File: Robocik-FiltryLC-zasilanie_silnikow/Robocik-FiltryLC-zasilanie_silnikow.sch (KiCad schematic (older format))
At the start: 18 parts, among them J1 XT90PW-F, J2 Conn_01x05, J3 Conn_01x03, J4 Conn_01x03, J5 Conn_01x03, J6 Conn_01x03, U1 ESC, U2 ESC, U3 ESC, U4 ESC

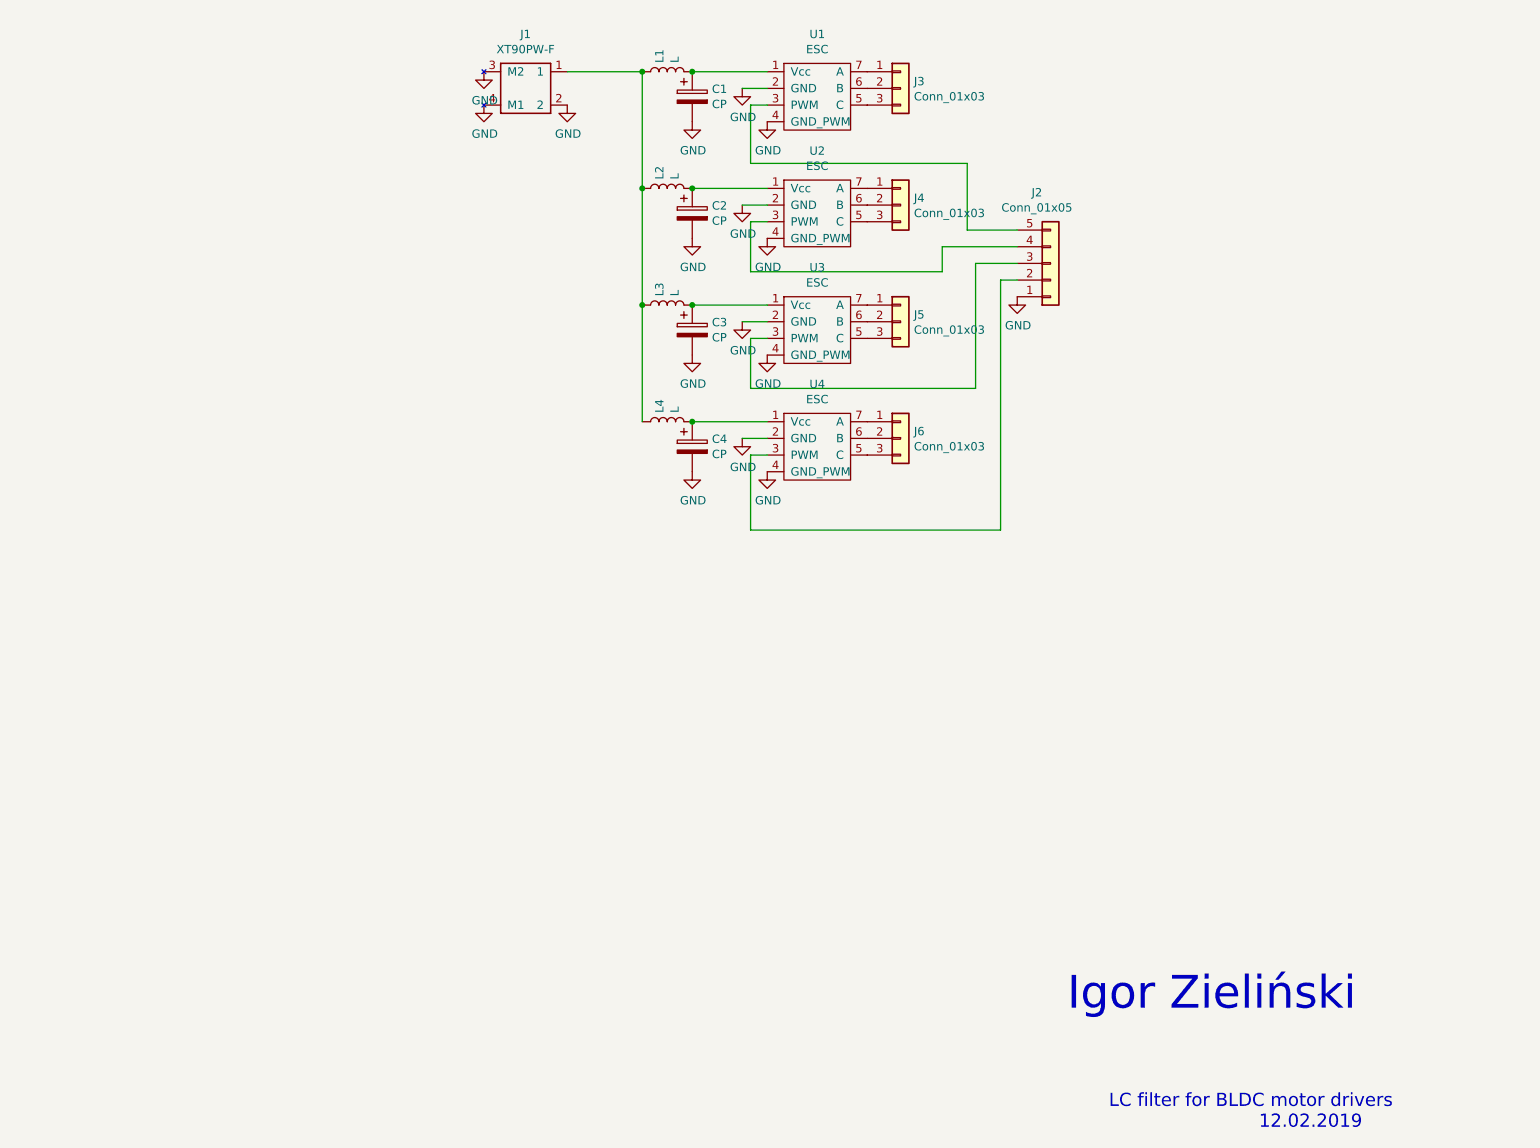
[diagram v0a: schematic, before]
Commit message: Added second board. Added 3D models to most elements. Included PCB top and botton jpg files. Resized PCB - from 12 x 17 cm to 10,5 x 12,5cm.
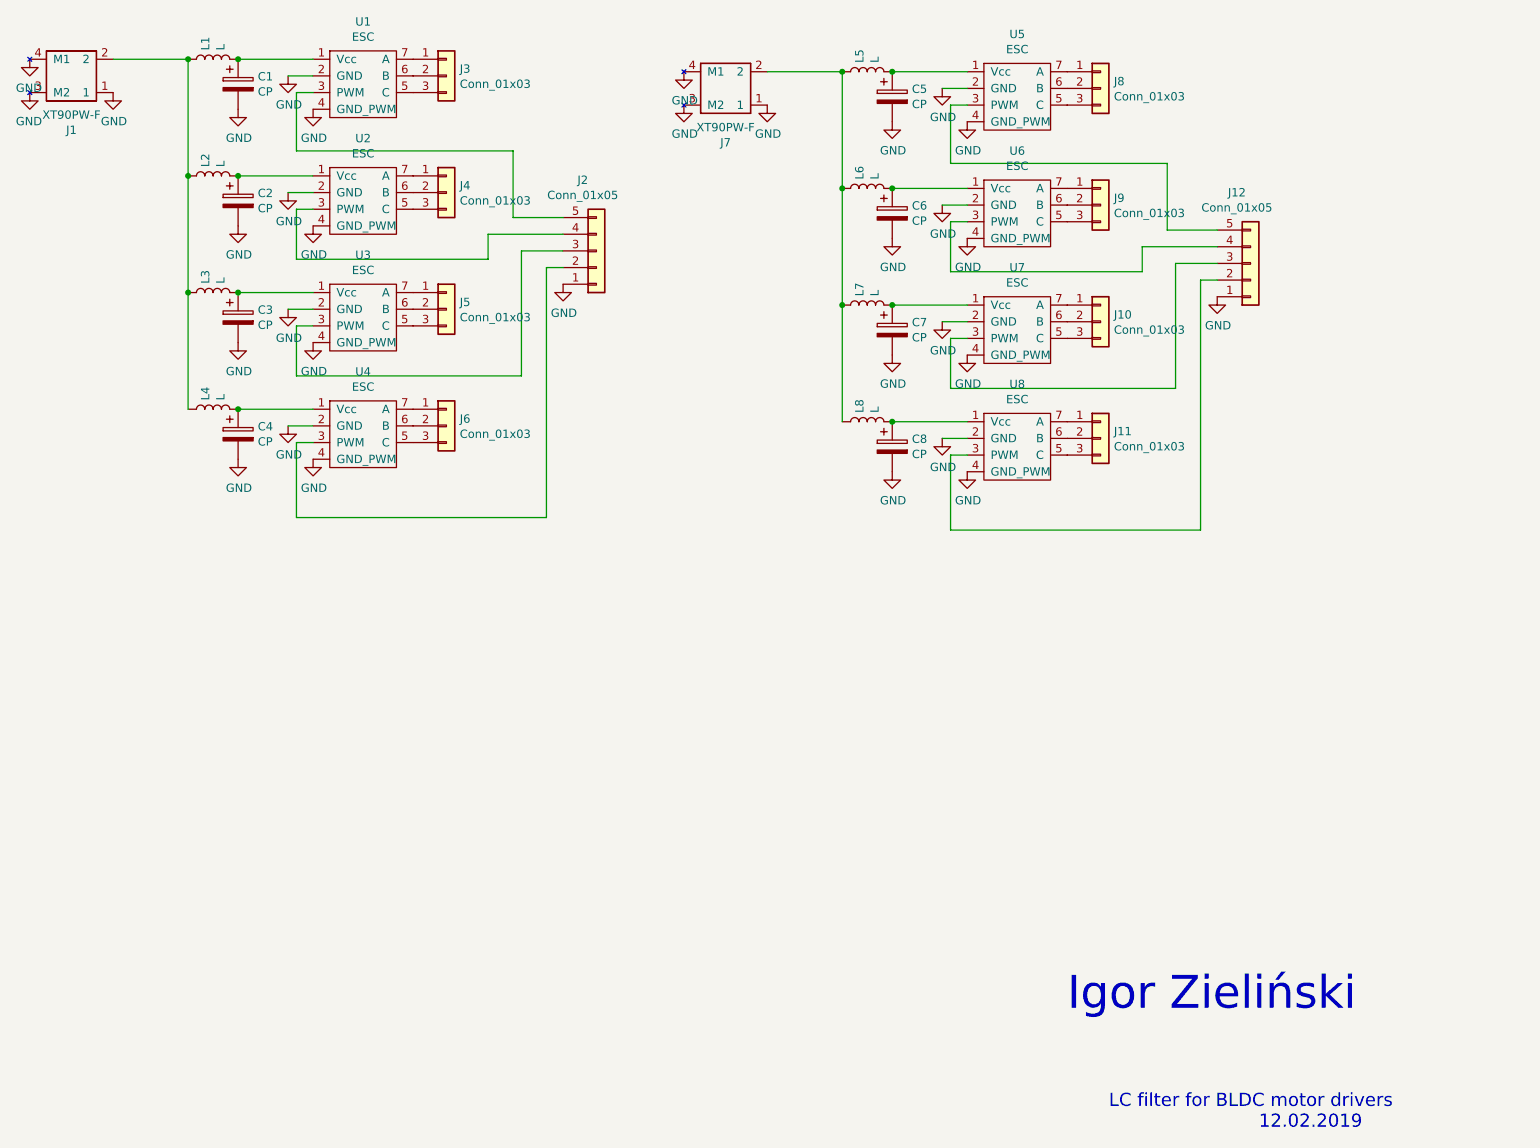
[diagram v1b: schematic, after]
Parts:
- added C5, C6, C7, C8: CP, Capacitor_THT:C_Radial_D10.0mm_H20.0mm_P5.00mm, symbol Device:CP
- added J10, J11, J8, J9: Conn_01x03, Connectors:MR30PW-FB, symbol Connector_Generic:Conn_01x03
- added J12: Conn_01x05, Connector_Molex:Molex_SPOX_5267-05A_1x05_P2.50mm_Vertical, symbol Connector_Generic:Conn_01x05
- added J7: XT90PW-F, Connectors:XT90PW-F, symbol Connectors:XT90PW-F
- added L5, L6, L7, L8: L, 74435571100:WE-HCI_189023, symbol Device:L
- added U5, U6, U7, U8: ESC, ESC:ESC, symbol ESC:ESC
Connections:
- net GND: now also J1.1, C5.2, C6.2, C7.2, C8.2, J12.1 (Pin_1), J7.1, J7.3 (M2), J7.4 (M1), U5.2 (GND), U5.4 (GND_PWM), U6.2 (GND), U6.4 (GND_PWM), U7.2 (GND), U7.4 (GND_PWM), U8.2 (GND), U8.4 (GND_PWM); no longer J1.2
- net at L1.1, L2.1, L3.1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: now also J1.2; no longer J1.1
- new net: C6.1, L6.2, U6.1 (Vcc)
- new net: J7.2, L5.1, L6.1, L7.1, L8.1
- new net: C7.1, L7.2, U7.1 (Vcc)
- new net: C8.1, L8.2, U8.1 (Vcc)
- new net: C5.1, L5.2, U5.1 (Vcc)
- new net: J12.5 (Pin_5), U5.3 (PWM)
- new net: J8.3 (Pin_3), U5.5 (C)
- new net: J8.2 (Pin_2), U5.6 (B)
- new net: J8.1 (Pin_1), U5.7 (A)
- new net: J12.4 (Pin_4), U6.3 (PWM)
- new net: J9.3 (Pin_3), U6.5 (C)
- new net: J9.2 (Pin_2), U6.6 (B)
- new net: J9.1 (Pin_1), U6.7 (A)
- new net: J12.3 (Pin_3), U7.3 (PWM)
- new net: J10.3 (Pin_3), U7.5 (C)
- new net: J10.2 (Pin_2), U7.6 (B)
- new net: J10.1 (Pin_1), U7.7 (A)
- new net: J12.2 (Pin_2), U8.3 (PWM)
- new net: J11.3 (Pin_3), U8.5 (C)
- new net: J11.2 (Pin_2), U8.6 (B)
- new net: J11.1 (Pin_1), U8.7 (A)
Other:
- moved on the sheet: C1, C2, C3, C4, J1, J2, J3, J4, J5, J6, L1, L2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

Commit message: Moved power connector to the side of the board. Added wiring for ESC output. Removed soldermask layers from high power lines.
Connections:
- net GND: now also J1.2; no longer J1.1
- net at L1.1, L2.1, L3.1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: now also J1.1; no longer J1.2
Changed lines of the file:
@@
 F 3 "" H 1125 1625 50  0001 C CNN
 	1    1125 1325
-	-1   0    0    1
+	-1   0    0    -1
 $EndComp
 $Comp
